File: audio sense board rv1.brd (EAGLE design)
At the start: 80 x 26.7 mm, 31 parts, among them IC2 TSOP38238, J1 PJRAN1X1U01X, J4 PJRAN1X1U01X, Q1 2N3904, Q2 2N3904

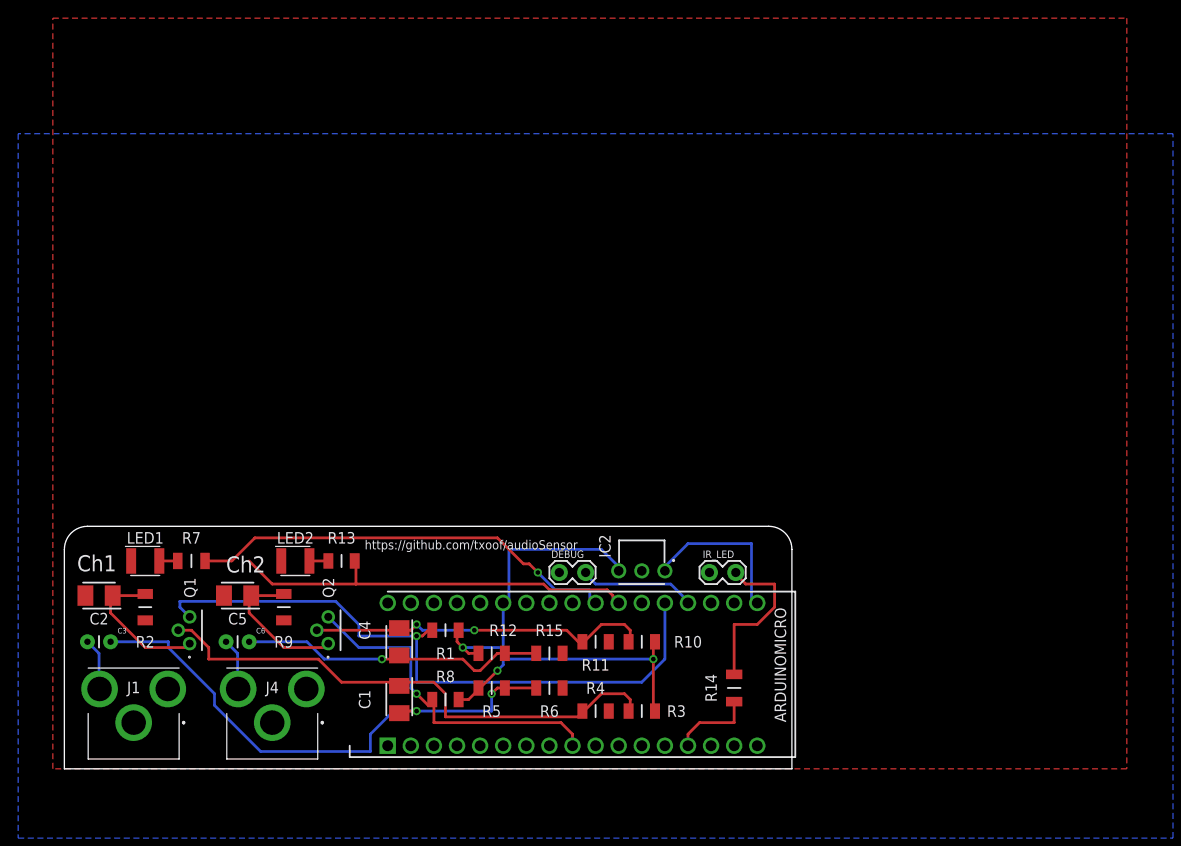
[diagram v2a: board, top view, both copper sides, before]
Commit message: add transformers
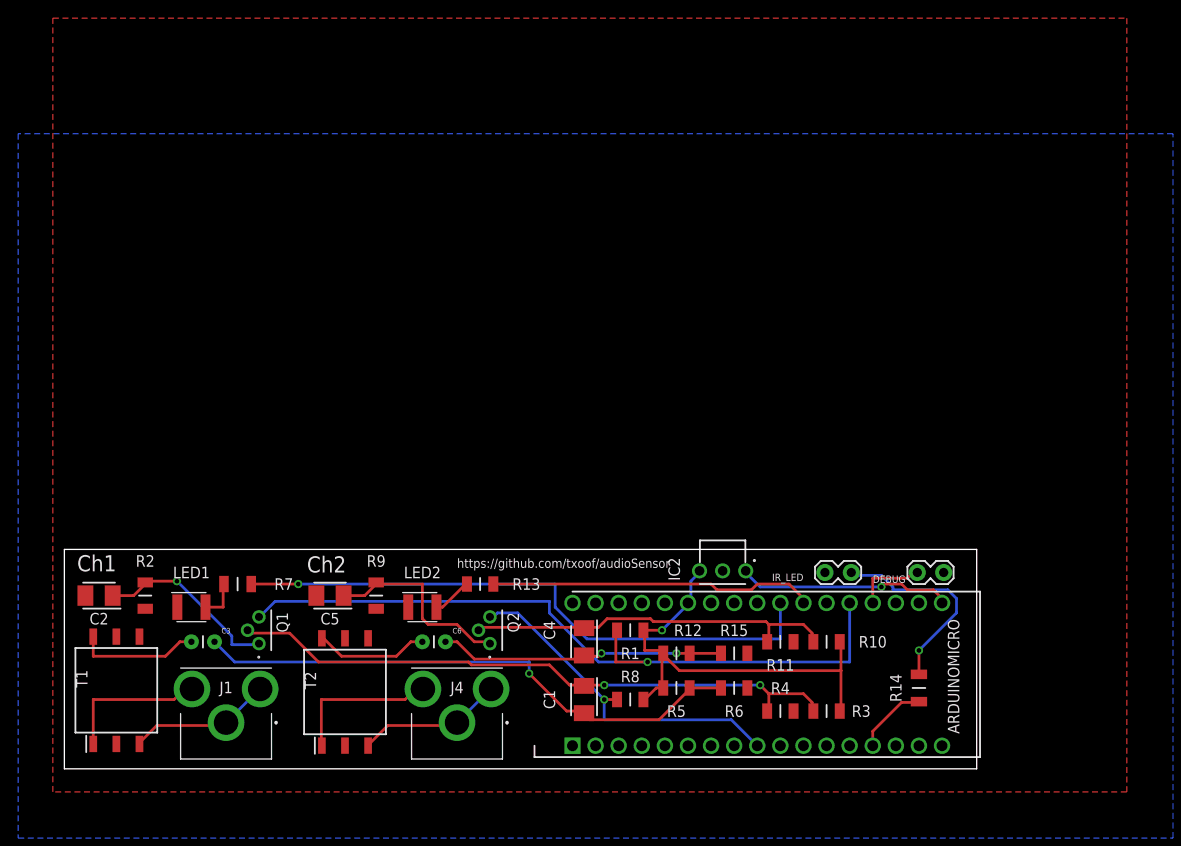
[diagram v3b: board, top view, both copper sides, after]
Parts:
- added T1, T2: 78601_9JC, Samac Populated:SOP254P1270X635-6N
- moved DEBUG 41.9 mm to (96.5, 21.6), turned to 180 degrees
- moved C6 21.6 mm to (40.6, 14.0)
- moved R14 20.3 mm to (94.0, 8.89)
- moved ARDUINOMICRO 20.3 mm to (55.9, 2.54)
- moved C1 20.3 mm to (57.1, 7.62)
- moved C4 20.3 mm to (57.1, 14.0)
- moved J4 20.3 mm to (43.2, 5.08)
- moved R1 20.3 mm to (62.2, 15.2)
- moved R12 20.3 mm to (67.3, 12.7)
- moved R5 20.3 mm to (67.3, 8.89)
- moved R8 20.3 mm to (62.2, 7.62)
- moved R10 20.3 mm to (83.8, 14.0)
- moved R11 20.3 mm to (78.7, 14.0)
- moved R15 20.3 mm to (73.7, 12.7)
- moved R3 20.3 mm to (83.8, 6.35)
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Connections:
- removed net N$16: C6.2, J4.2
- new net N$10: C6.2, T2.6
- new net N$11: J1.1, J1.3, T1.3
- new net N$13: C3.2, T1.6
- new net N$5: J4.1, J4.3, T2.3
- new net N$8: J4.2, T2.1
- net GND: now also T1.4, T2.4; no longer J1.1, J1.3, J4.1, J4.3
- net N$6: now also T1.1; no longer C3.2
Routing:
- net STATUS_CH1: track 48.4 -> 66.1 mm
- net N$8: track 0.00 -> 16.8 mm
- net VCC: track 66.7 -> 50.4 mm, vias 3 -> 1
- net N$5: track 0.00 -> 16.1 mm
- net N$11: track 0.00 -> 15.8 mm
- net N$13: track 0.00 -> 13.6 mm
- net N$10: track 0.00 -> 12.5 mm
- net CHAN1: track 72.1 -> 82.8 mm
- net N$6: track 5.73 -> 16.3 mm
- net STATUS_CH2: track 45.7 -> 35.8 mm
- net N$3: track 59.2 -> 68.6 mm, vias 0 -> 2
- net N$16: track 5.73 -> 0.00 mm
- net N$19: track 16.4 -> 21.8 mm
- net DEBUGJ: track 13.1 -> 7.88 mm
- net IRREC: track 18.7 -> 23.7 mm, vias 0 -> 1
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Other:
- board size 80 x 26.7 mm -> 100.3 x 24.1 mm

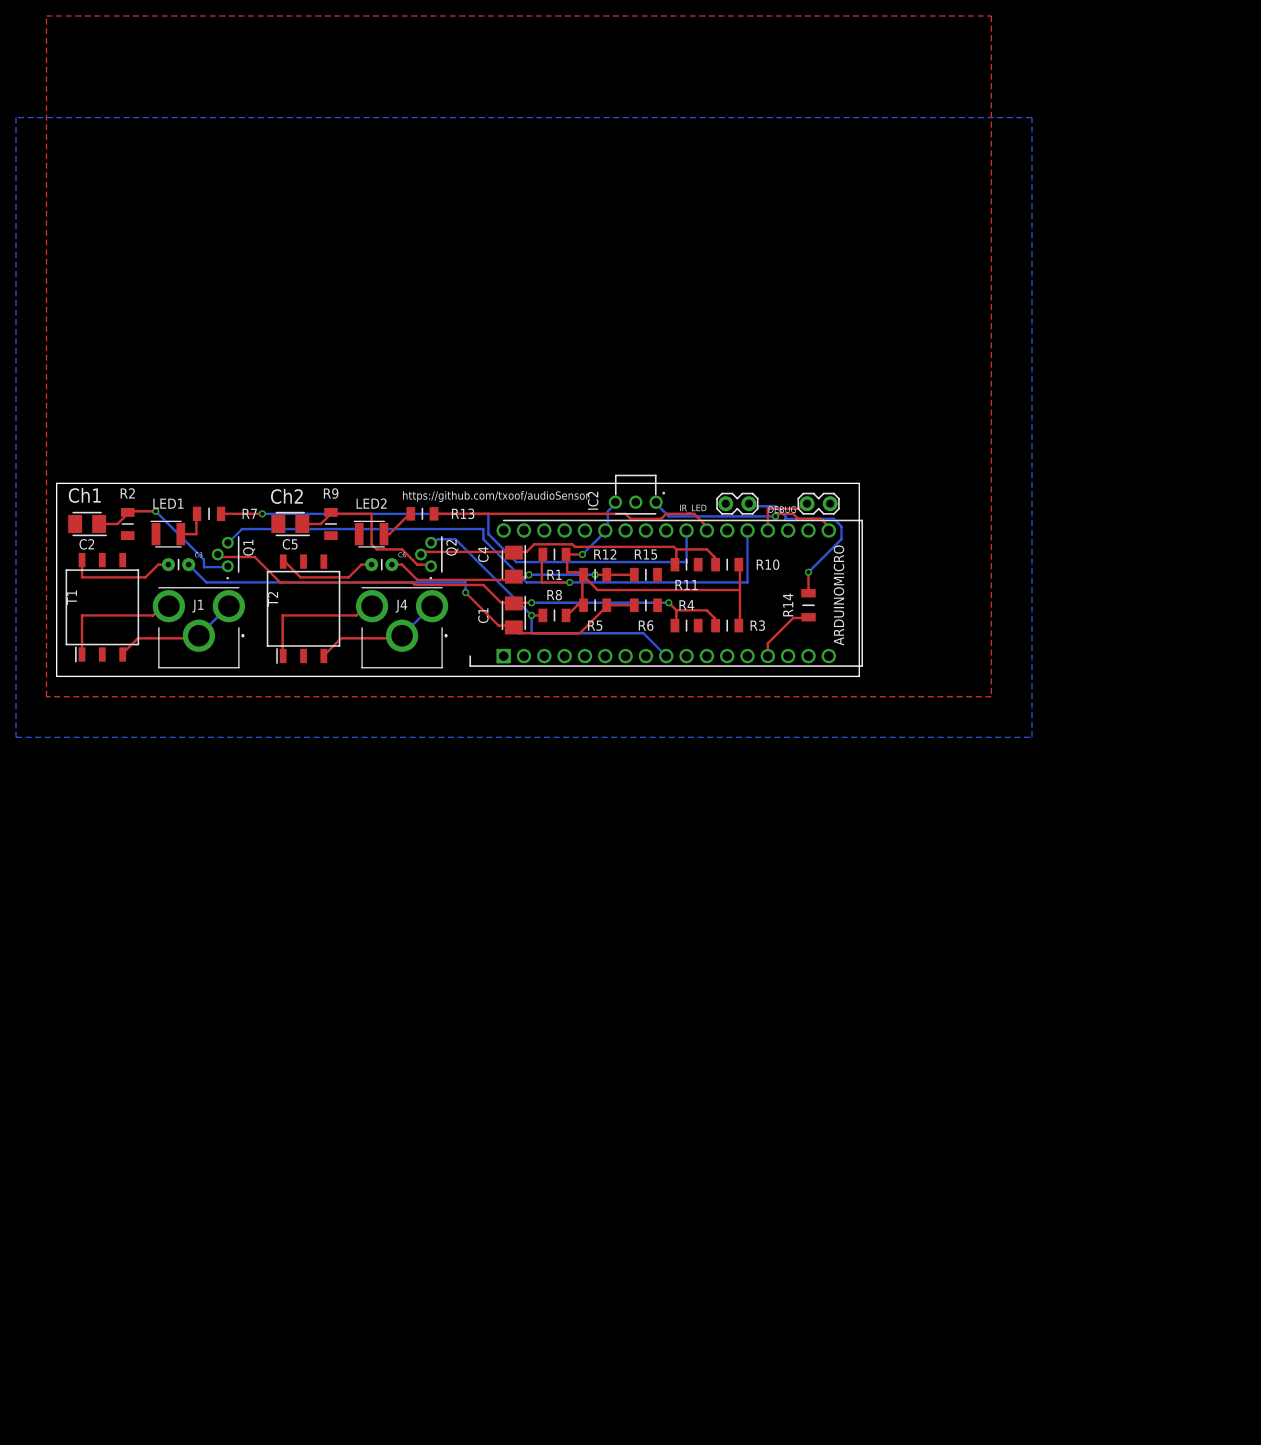
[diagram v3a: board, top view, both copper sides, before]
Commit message: correcting issue - voltage divider in wrong location in both channels
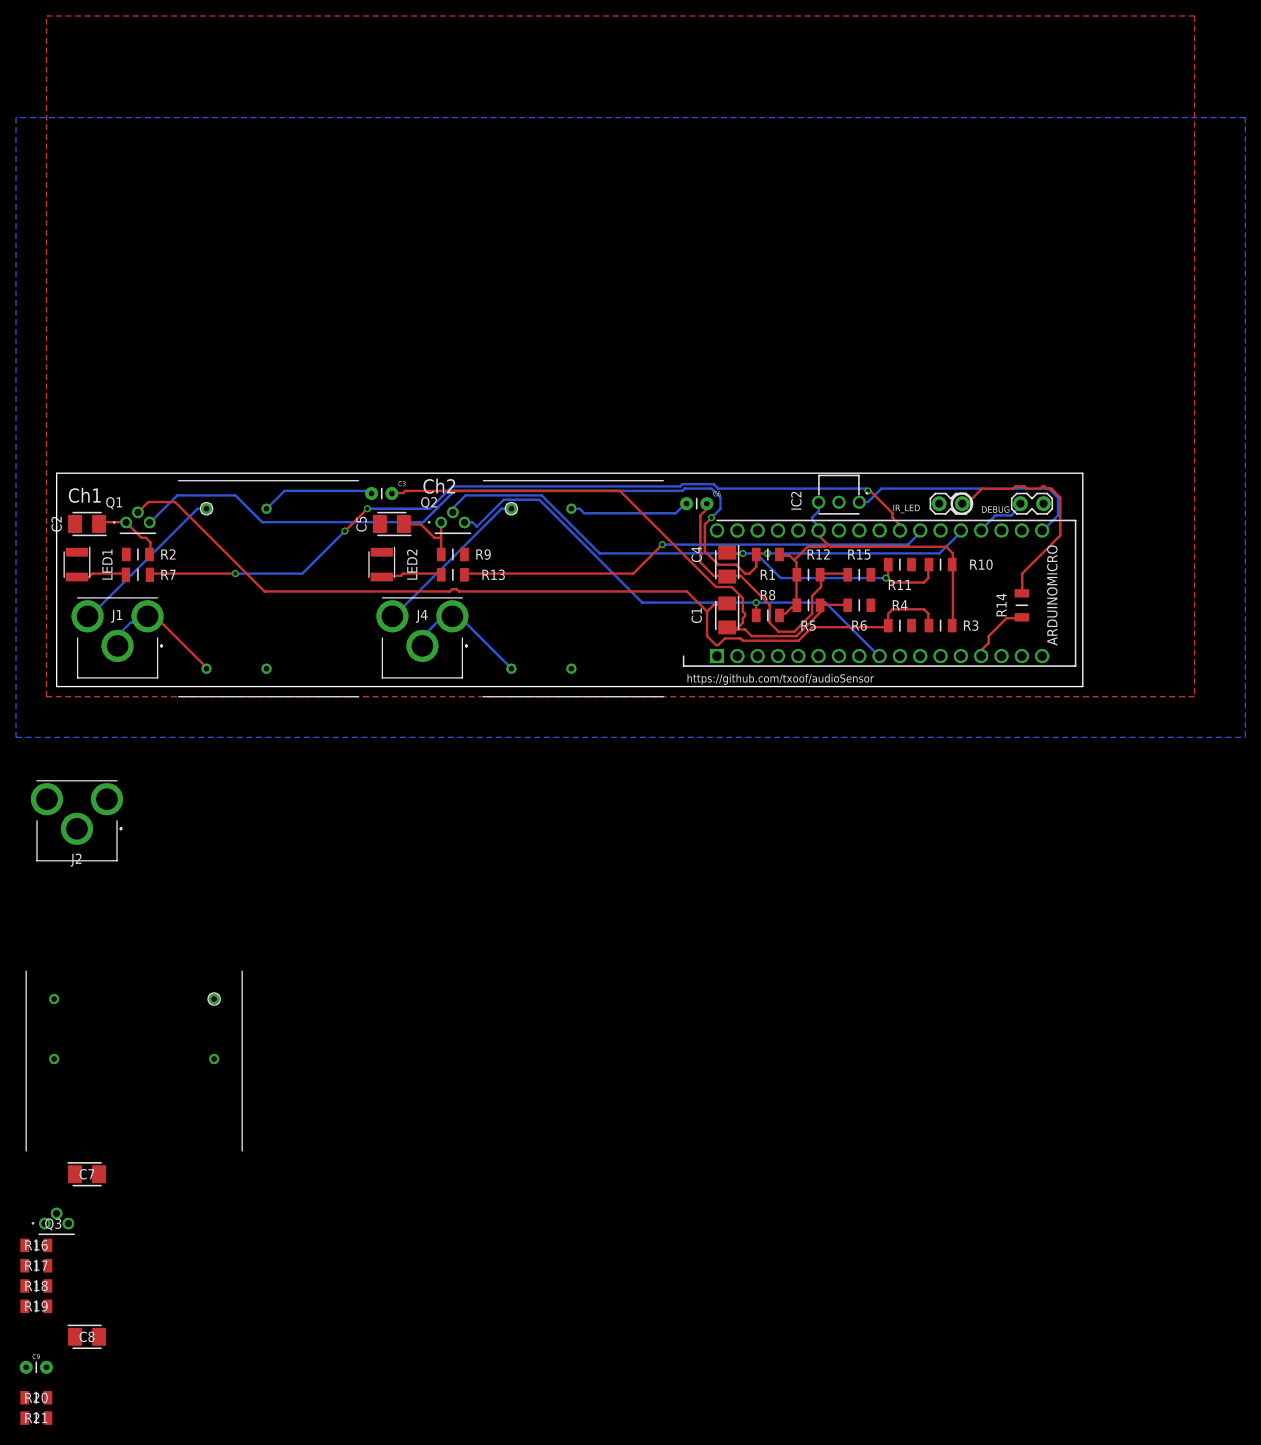
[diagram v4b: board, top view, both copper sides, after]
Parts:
- removed T1, T2: 78601_9JC, Samac Populated:SOP254P1270X635-6N
- added C7, C8: TAJB226M010RNJ, Samac Populated:CAPPM3528X210N
- added C9: 1uF, SparkFun-Capacitors:CAP-PTH-2.54
- added J2: PJRAN1X1U01X, Samac Populated:PJRAN1X1U01X
- added L1, L2, L3: IT237, My Library:IT237
- added Q3: 2N3904, Samac Populated:CS_TO-92
- added R16: 1K, Samac Populated:RESC3116X70N
- added R17: 100, Samac Populated:RESC3116X70N
- added R18: 39K, Samac Populated:RESC3116X70N
- added R19, R20, R21: 10K, Samac Populated:RESC3116X70N
- moved C6 40.1 mm to (80.0, 21.6)
- moved C3 26.9 mm to (40.6, 22.9)
- moved R1 26.7 mm to (88.9, 15.2)
- moved R8 26.7 mm to (88.9, 7.62)
- moved DEBUG 26.7 mm to (123.2, 21.6)
- moved IR_LED 26.7 mm to (113.0, 21.6)
- moved R10 26.7 mm to (110.5, 14.0)
- moved R11 26.7 mm to (105.4, 14.0)
- moved R12 26.7 mm to (94.0, 12.7)
- moved R14 26.7 mm to (120.7, 8.89)
- moved R15 26.7 mm to (100.3, 12.7)
- moved R3 26.7 mm to (110.5, 6.35)
- moved R4 26.7 mm to (105.4, 6.35)
- moved R5 26.7 mm to (94.0, 8.89)
- moved R6 26.7 mm to (100.3, 8.89)
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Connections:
- new net N$12: J2.1, J2.3, L3.2
- new net N$15: J2.2, L3.1
- new net N$16: C7.1, Q3.2, R18.1, R19.1
- new net N$17: C7.2, L3.3
- new net N$20: C8.1, Q3.1, R17.1
- new net N$21: C9.2, Q3.3, R16.1
- net CHAN1: now also C9.1, R20.1, R21.2
- net GND: now also C8.2, L1.4, L2.4, L3.4, R17.2, R19.2, R21.1; no longer T1.4, T2.4
- net N$10: now also C3.2, L1.3; no longer C6.2, T2.6
- net N$11: now also L1.2; no longer T1.3
- net N$13: now also C6.2, L2.3; no longer C3.2, T1.6
- net N$5: now also L2.2; no longer T2.3
- net N$6: now also L1.1; no longer T1.1
- net N$8: now also L2.1; no longer T2.1
- net VCC: now also R16.2, R18.2, R20.2
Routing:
- net N$3: track 68.6 -> 116.6 mm, vias 2 -> 0
- net CHAN1: track 82.8 -> 120.5 mm, vias 1 -> 2
- net STATUS_CH1: track 66.1 -> 101.6 mm, vias 1 -> 4
- net N$14: track 41.1 -> 70.9 mm, vias 0 -> 2
- net CHAN2: track 38.5 -> 63.2 mm
- net STATUS_CH2: track 35.8 -> 59.6 mm, vias 0 -> 1
- net N$19: track 21.8 -> 9.35 mm
- net N$7: track 61.8 -> 73.1 mm, vias 1 -> 0
- net N$1: track 20.4 -> 9.30 mm, vias 1 -> 0
- net IRREC: track 23.7 -> 31.1 mm, vias 1 -> 0
- net N$18: track 31.4 -> 36.5 mm, vias 2 -> 0
- net N$9: track 23.2 -> 27.9 mm, vias 1 -> 0
- net N$6: track 16.3 -> 20.7 mm
- net N$8: track 16.8 -> 20.4 mm
- net N$2: track 4.40 -> 7.75 mm
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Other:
- board size 100.3 x 24.1 mm -> 128.3 x 26.7 mm

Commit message: remove improper components, rework circuit
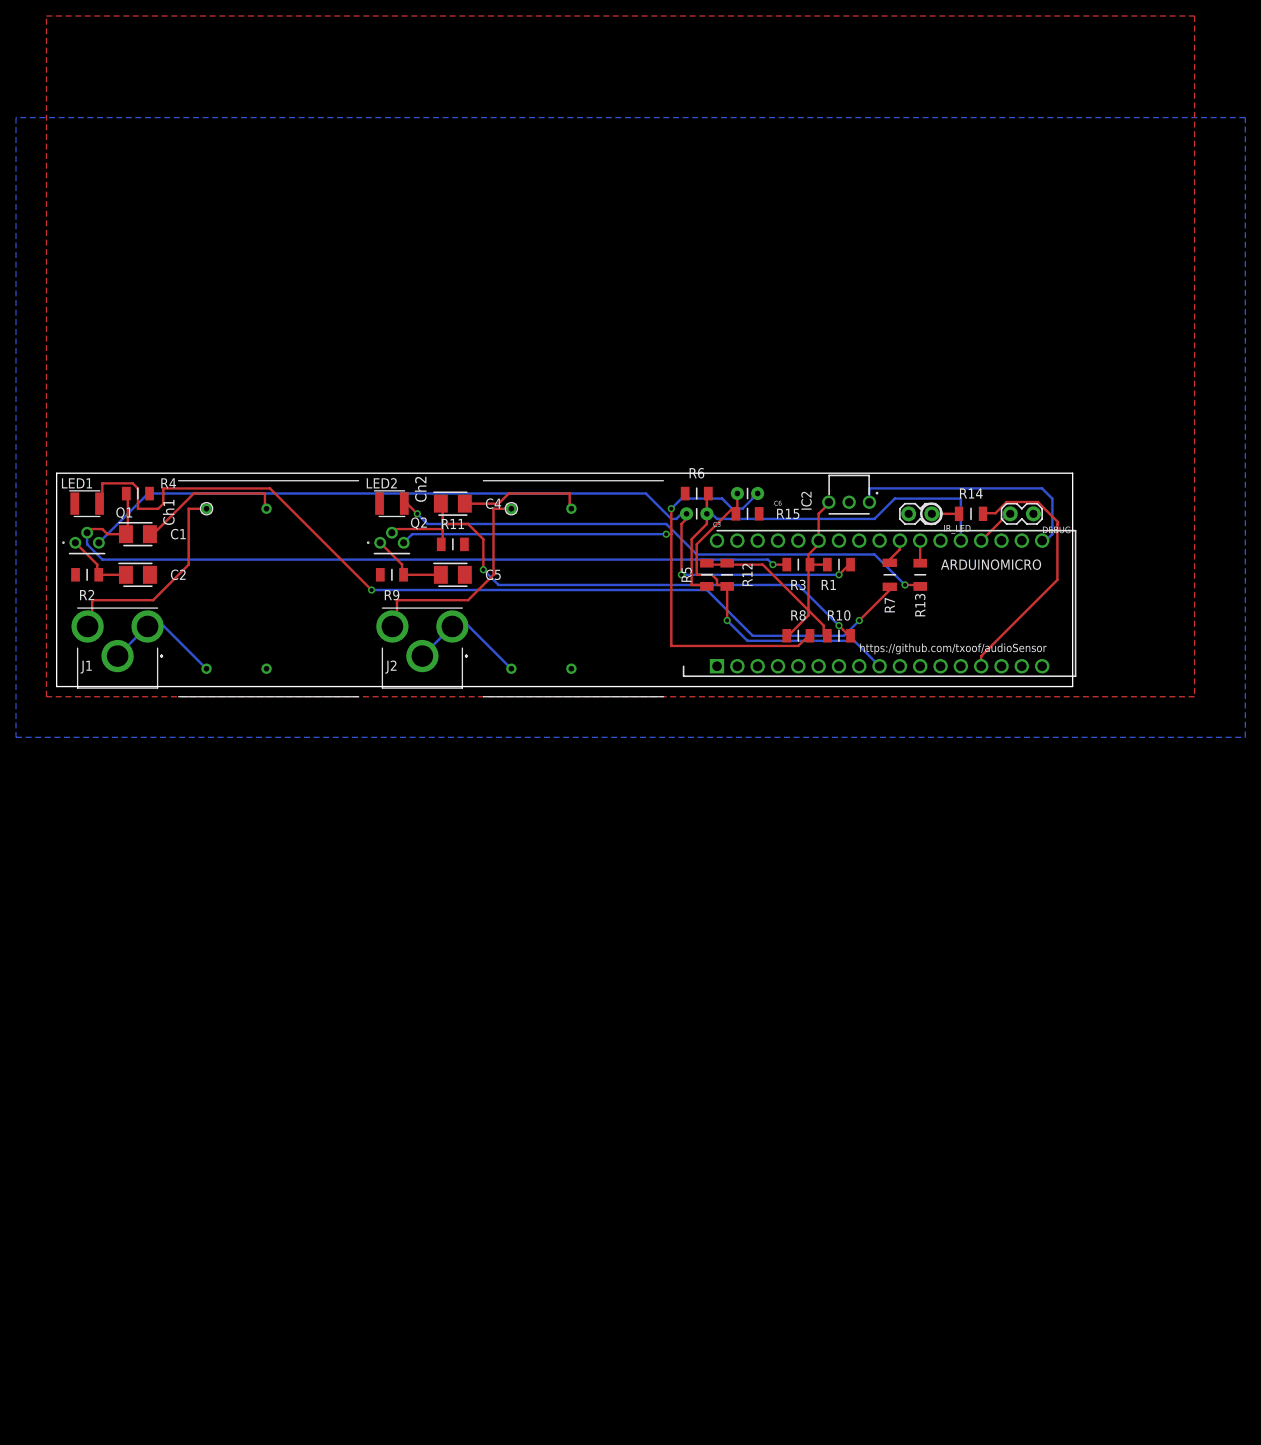
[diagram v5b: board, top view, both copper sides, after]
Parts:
- removed C7, C8: TAJB226M010RNJ, Samac Populated:CAPPM3528X210N
- removed C9: 1uF, SparkFun-Capacitors:CAP-PTH-2.54
- removed J4: PJRAN1X1U01X, Samac Populated:PJRAN1X1U01X
- removed L3: IT237, My Library:IT237
- removed Q3: 2N3904, Samac Populated:CS_TO-92
- removed R16: 1K, Samac Populated:RESC3116X70N
- removed R17: 100, Samac Populated:RESC3116X70N
- removed R18: 39K, Samac Populated:RESC3116X70N
- removed R19, R20, R21: 10K, Samac Populated:RESC3116X70N
- moved R4 96.7 mm to (10.2, 22.9)
- moved R7 94.0 mm to (104.1, 12.7), turned to 90 degrees
- moved C1 74.4 mm to (10.2, 17.8), turned to 0 degrees
- moved R13 58.4 mm to (108.0, 12.7), turned to 90 degrees
- moved R11 55.9 mm to (49.5, 16.5)
- moved J2 48.3 mm to (45.7, 2.54)
- moved C3 39.5 mm to (80.0, 20.3)
- moved C4 35.1 mm to (49.5, 21.6), turned to 0 degrees
- moved R6 24.7 mm to (80.0, 22.9)
- moved R3 19.3 mm to (92.7, 14.0)
- moved R15 15.9 mm to (86.4, 20.3), turned to 180 degrees
- moved R10 15.5 mm to (97.8, 5.08), turned to 180 degrees
- moved R5 13.3 mm to (81.3, 12.7), turned to 90 degrees
- moved R14 13.1 mm to (114.3, 20.3), turned to 0 degrees
- moved R12 10.2 mm to (83.8, 12.7), turned to 90 degrees
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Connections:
- removed net N$10: C3.2, L1.3
- removed net N$12 (its old number): J2.1, J2.3, L3.2
- removed net N$13: C6.2, L2.3
- removed net N$15 (its old number): J2.2, L3.1
- removed net N$16 (its old number): C7.1, Q3.2, R18.1, R19.1
- removed net N$18: C4.2, C6.1, R12.1, R15.1
- removed net N$20 (its old number): C8.1, Q3.1, R17.1
- removed net N$7 (its old number): C1.2, C3.1, R5.1, R6.1
- new net N$1: J2.1, J2.3, L2.2
- new net N$3: J2.2, L2.1
- net CHAN1: now also C3.1, R5.1, R6.2; no longer C9.1, Q1.3, R1.1, R20.1, R21.2
- net CHAN2: now also C6.1, R12.1, R15.2; no longer Q2.3, R8.1
- net GND: now also R15.1, R6.1; no longer C8.2, L3.4, R15.2, R17.2, R19.2, R21.1, R6.2
- net N$17: now also C1.2, L1.3; no longer C7.2, L3.3
- net N$21: now also C3.2, Q1.3, R1.1; no longer C9.2, Q3.3, R16.1
- net N$5: now also C4.2, L2.3; no longer J4.1, J4.3, L2.2
- net N$8: now also C6.2, Q2.3, R8.1; no longer J4.2, L2.1
- net VCC: no longer R16.2, R18.2, R20.2
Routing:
- net N$4: track 6.42 -> 116.7 mm, vias 0 -> 2
- net N$21: track 0.00 -> 107.1 mm, vias 0 -> 2
- net STATUS_CH1: track 101.6 -> 3.30 mm, vias 4 -> 0
- net N$7 (its old number): track 73.1 -> 0.00 mm
- net CHAN1: track 120.5 -> 52.8 mm, vias 2 -> 0
- net N$8: track 20.4 -> 81.9 mm, vias 0 -> 2
- net N$2: track 7.75 -> 68.9 mm, vias 0 -> 2
- net STATUS_CH2: track 59.6 -> 2.82 mm, vias 1 -> 0
- net N$18: track 36.5 -> 0.00 mm
- net N$3: track 0.00 -> 27.6 mm
- net IRLED: track 7.95 -> 33.1 mm
- net N$9: track 27.9 -> 3.40 mm
- net CHAN2: track 63.2 -> 44.7 mm
- net N$17: track 0.00 -> 18.4 mm
- net N$16: track 116.6 -> 101.0 mm, vias 0 -> 1
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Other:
- board size 128.3 x 26.7 mm -> 127 x 26.7 mm
